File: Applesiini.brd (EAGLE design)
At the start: 63 x 69 mm, 55 parts

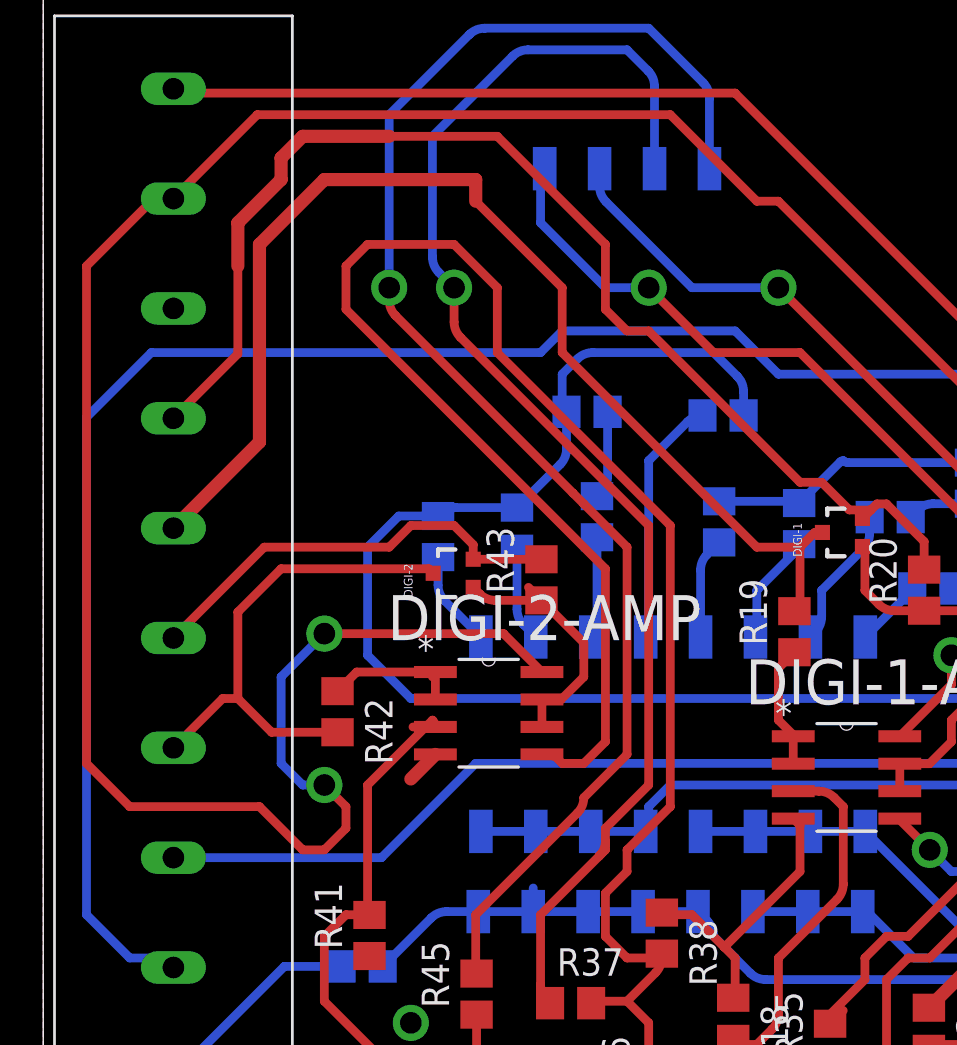
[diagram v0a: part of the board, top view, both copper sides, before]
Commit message: add correction to "Appelsiini" board
adds tolerance to one connection
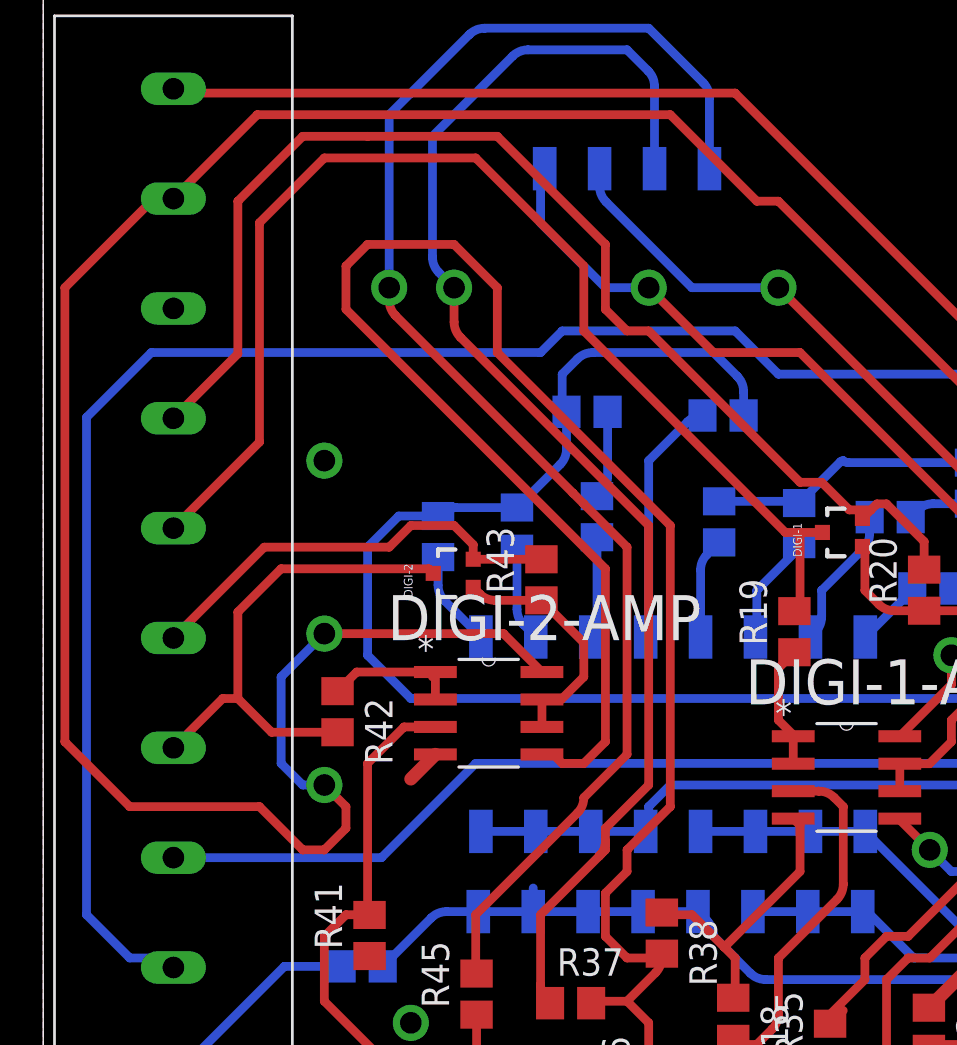
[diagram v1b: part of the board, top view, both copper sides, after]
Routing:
- net DIGI_LOW_1: track 56.9 -> 55.9 mm
- net DIGI_HIGH_1: track 54.8 -> 55.7 mm
- net N$64: track 12.2 -> 11.3 mm
- net VCC: track 216.3 -> 217.1 mm
- net N$11: track 33.0 -> 32.2 mm
- net GND: vias 6 -> 7

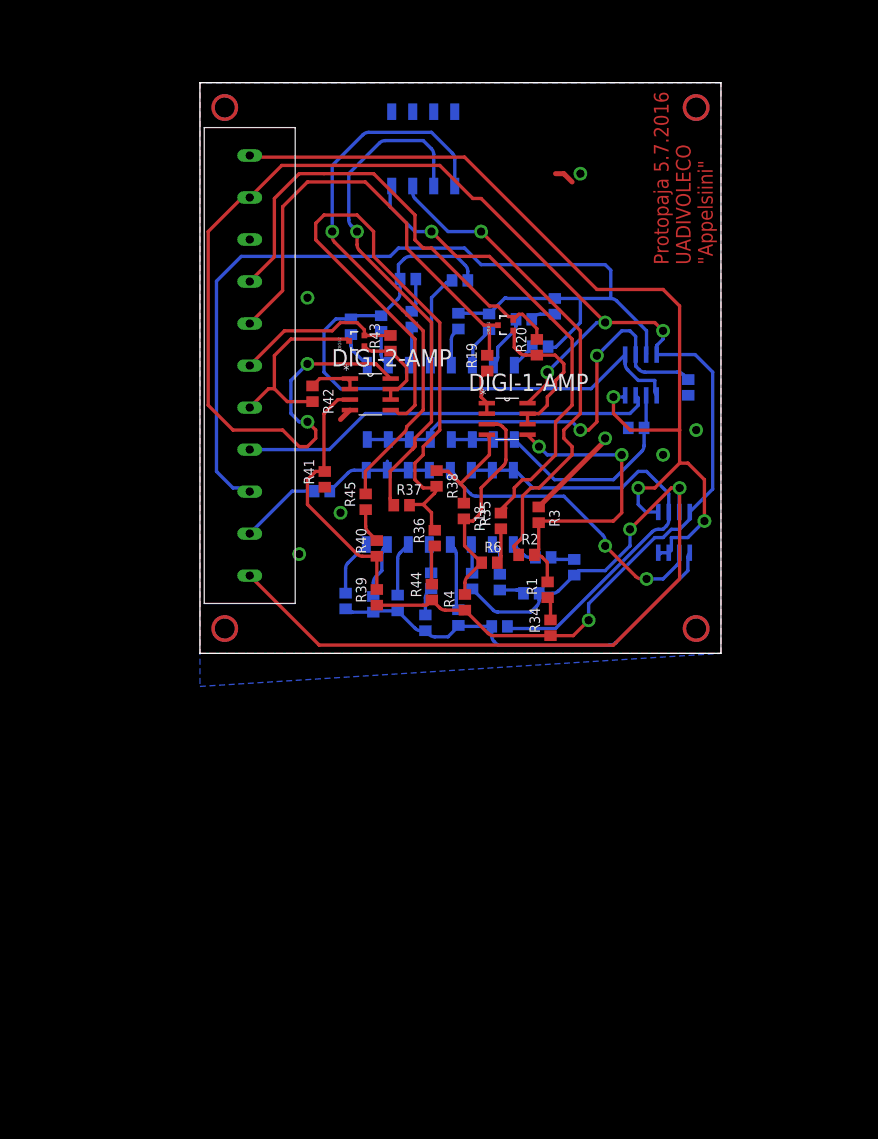
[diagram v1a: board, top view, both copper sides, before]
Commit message: add correction to "Appelsiini" board
gives more space around the board for easier matching of board sides.
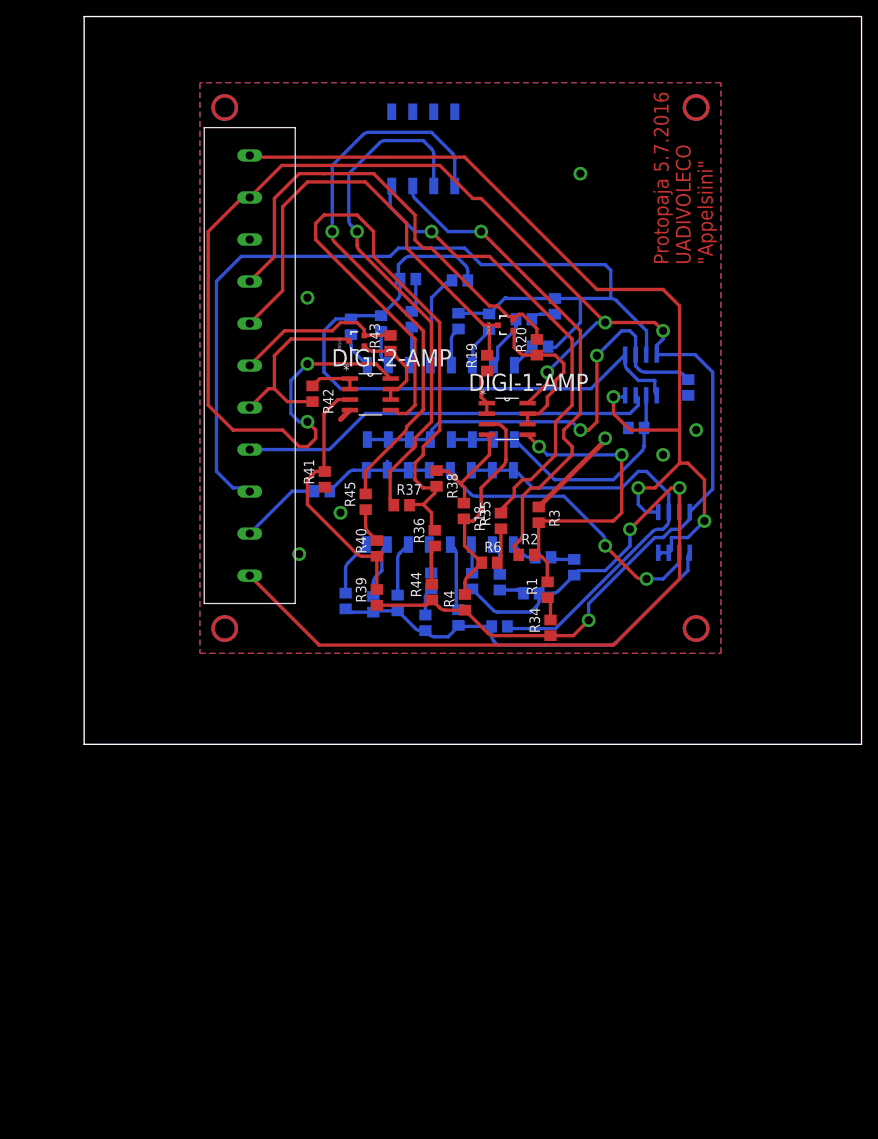
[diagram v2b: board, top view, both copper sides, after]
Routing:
- net GND: track 29.6 -> 27.2 mm
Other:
- board size 63 x 69 mm -> 94 x 88 mm
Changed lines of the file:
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@@
 <layer number="17" name="Pads" color="2" fill="1" visible="yes" active="yes"/>
 <layer number="18" name="Vias" color="2" fill="1" visible="yes" active="yes"/>
-<layer number="19" name="Unrouted" color="6" fill="1" visible="yes" active="yes"/>
+<layer number="19" name="Unrouted" color="6" fill="1" visible="no" active="yes"/>
 <layer number="20" name="Dimension" color="15" fill="1" visible="yes" active="yes"/>
 <layer number="21" name="tPlace" color="7" fill="1" visible="no" active="yes"/>
@@
 <board>
 <plain>
-<wire x1="0" y1="3" x2="63" y2="3" width="0" layer="20"/>
-<wire x1="63" y1="3" x2="63" y2="72" width="0" layer="20"/>
-<wire x1="63" y1="72" x2="0" y2="72" width="0" layer="20"/>
-<wire x1="0" y1="72" x2="0" y2="3" width="0" layer="20"/>
+<wire x1="-14" y1="-8" x2="80" y2="-8" width="0" layer="20"/>
+<wire x1="80" y1="-8" x2="80" y2="80" width="0" layer="20"/>
+<wire x1="80" y1="80" x2="-14" y2="80" width="0" layer="20"/>
+<wire x1="-14" y1="80" x2="-14" y2="-8" width="0" layer="20"/>
 <text x="62" y="50" size="1.778" layer="1" rot="R90">Protopaja 5.7.2016
 UADIVOLECO
@@
 <vertex x="63" y="72"/>
 </polygon>
-<wire x1="43" y1="61" x2="44" y2="61" width="0.6096" layer="1"/>
-<wire x1="44" y1="61" x2="45" y2="60" width="0.6096" layer="1"/>
 <wire x1="18.1362" y1="32.415" x2="17" y2="31.2788" width="0.6096" layer="1"/>
 <wire x1="40.96" y1="20.7" x2="49" y2="28.74" width="0.6096" layer="1"/>
@@
 <polygon width="0.254" layer="16" spacing="0.254" isolate="0.6096">
 <vertex x="0" y="72"/>
-<vertex x="0" y="-1"/>
+<vertex x="0" y="3"/>
 <vertex x="63" y="3"/>
 <vertex x="63" y="72"/>

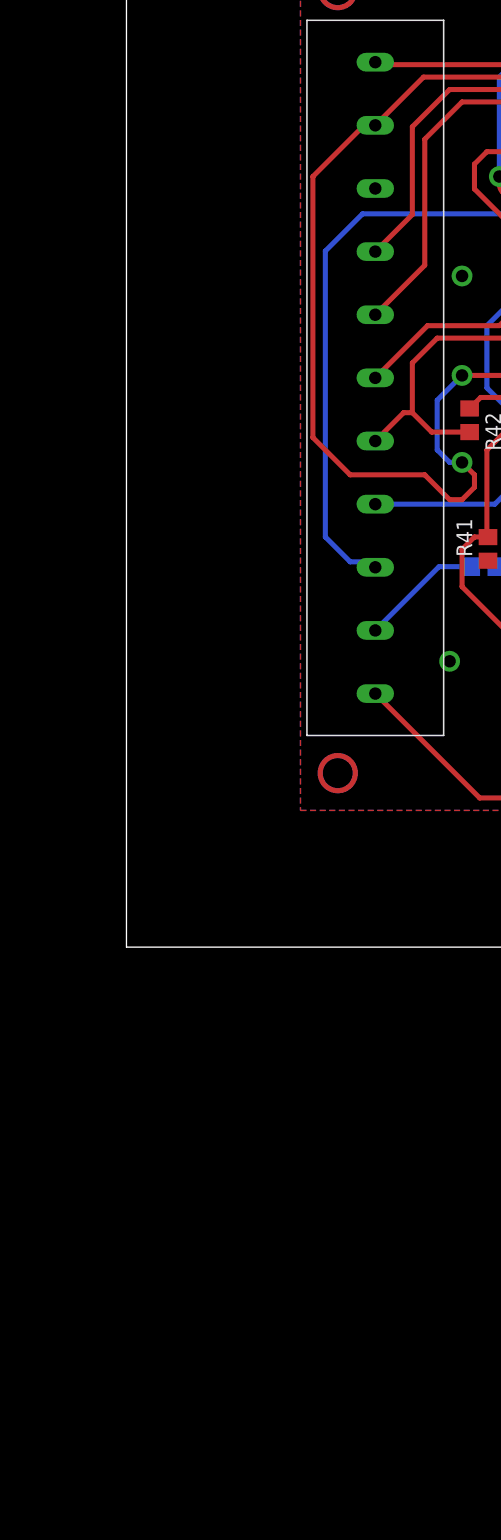
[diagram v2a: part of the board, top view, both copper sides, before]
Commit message: begin lime-lemon schematic and board
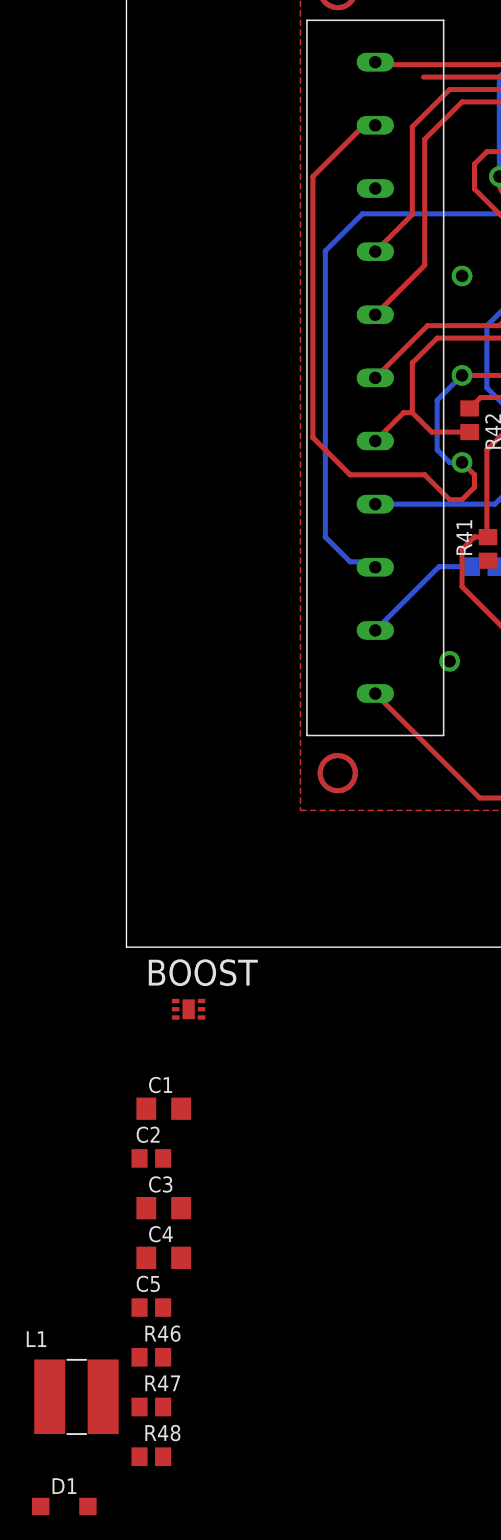
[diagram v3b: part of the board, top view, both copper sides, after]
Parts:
- added BOOST: TPS61170DRVT, Texas Instruments_By_element14_Batch_1:SON65P210X210X80-7N
- added C1, C3, C4: (no value), rcl:C1206
- added C2, C5: (no value), rcl:C0805
- added D1: (no value), diode:SOD123
- added L1: 22uH, SparkFun-Passives:SRN6045
- added R46, R47, R48: (no value), rcl:R0805
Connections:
- new net +5V: BOOST.5, BOOST.6, C2.1, L1.2, U$1.P$1
- new net N$44: BOOST.4, D1.A, L1.1
- new net N$47: D1.C, R47.2
- new net N$49: BOOST.2, R48.2
- new net N$51: C5.1, R48.1
- net GND: now also BOOST.3, C1.2, C2.2, C3.2, C4.2, C5.2, R46.2
- net VCC: now also BOOST.1, C1.1, C3.1, C4.1, R46.1, R47.1; no longer U$1.P$1
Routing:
- net VCC: track 217.1 -> 210.8 mm
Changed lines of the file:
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@@
 <element name="U$1" library="ruuviliitin" package="10KPL508" value="5.08PITCHTERMINAL" x="6.02" y="37.8" rot="R270"/>
 <element name="S4" library="smd-special" package="SMS-004" value="SWS004" x="27" y="64" rot="MR180"/>
+<element name="BOOST" library="Texas Instruments_By_element14_Batch_1" package="SON65P210X210X80-7N" value="TPS61170DRVT" x="-9" y="-13">
+<attribute name="PACKAGE" value="SON-6" x="-9" y="-13" size="1.778" layer="27" display="off"/>
+<attribute name="OC_FARNELL" value="1703404" x="-9" y="-13" size="1.778" layer="27" display="off"/>
+<attribute name="MPN" value="TPS61170DRVT" x="-9" y="-13" size="1.778" layer="27" display="off"/>
+<attribute name="SUPPLIER" value="Texas Instruments" x="-9" y="-13" size="1.778" layer="27" display="off"/>
+<attribute name="OC_NEWARK" value="65M6342" x="-9" y="-13" size="1.778" layer="27" display="off"/>
+</element>
+<element name="C1" library="rcl" package="C1206" value="" x="-11" y="-21"/>
+<element name="C2" library="rcl" package="C0805" value="" x="-12" y="-25"/>
+<element name="C3" library="rcl" package="C1206" value="" x="-11" y="-29"/>
+<element name="C4" library="rcl" package="C1206" value="" x="-11" y="-33"/>
+<element name="C5" library="rcl" package="C0805" value="" x="-12" y="-37"/>
+<element name="R46" library="rcl" package="R0805" value="" x="-12" y="-41"/>
+<element name="R47" library="rcl" package="R0805" value="" x="-12" y="-45"/>
+<element name="R48" library="rcl" package="R0805" value="" x="-12" y="-49"/>
+<element name="L1" library="SparkFun-Passives" package="SRN6045" value="22uH" x="-18" y="-44">
+<attribute name="PROD_ID" value="NDUC-11627" x="-18" y="-44" size="1.778" layer="27" display="off"/>
+</element>
+<element name="D1" library="diode" package="SOD123" value="" x="-19" y="-53"/>
 </elements>
 <signals>
@@
 <via x="56" y="27" extent="1-16" drill="1" diameter="1.6764"/>
 <via x="13" y="46" extent="1-16" drill="1" diameter="1.6764"/>
+<contactref element="C5" pad="2"/>
+<contactref element="C2" pad="2"/>
+<contactref element="BOOST" pad="3"/>
+<contactref element="R46" pad="2"/>
+<contactref element="C4" pad="2"/>
+<contactref element="C3" pad="2"/>
+<contactref element="C1" pad="2"/>
+<wire x1="30.81" y1="68.4958" x2="46" y2="61" width="0" layer="19" extent="16-16"/>
+<wire x1="28.27" y1="68.4958" x2="30.81" y2="68.4958" width="0" layer="19" extent="16-16"/>
+<wire x1="25.73" y1="68.4958" x2="28.27" y2="68.4958" width="0" layer="19" extent="16-16"/>
+<wire x1="23.19" y1="68.4958" x2="25.73" y2="68.4958" width="0" layer="19" extent="16-16"/>
+<wire x1="6.02" y1="53.04" x2="23.19" y2="68.4958" width="0" layer="19" extent="16-16"/>
+<wire x1="13" y1="46" x2="6.02" y2="53.04" width="0" layer="19" extent="1-1"/>
+<wire x1="18.1362" y1="32.415" x2="13" y2="46" width="0" layer="19" extent="1-1"/>
+<wire x1="15.09" y1="23.09" x2="17" y2="31.2788" width="0" layer="19" extent="1-1"/>
+<wire x1="17" y1="20" x2="15.09" y2="23.09" width="0" layer="19" extent="1-1"/>
+<wire x1="12" y1="15" x2="17" y2="20" width="0" layer="19" extent="1-1"/>
+<wire x1="28.61" y1="25.1" x2="17" y2="20" width="0" layer="19" extent="1-1"/>
+<wire x1="40.96" y1="20.7" x2="35" y2="27" width="0" layer="19" extent="1-1"/>
+<wire x1="51.8" y1="30.26" x2="49" y2="29" width="0" layer="19" extent="16-16"/>
+<wire x1="56" y1="27" x2="51.8" y2="30.26" width="0" layer="19" extent="16-16"/>
+<wire x1="60" y1="30" x2="56" y2="27" width="0" layer="19" extent="1-1"/>
+<wire x1="59.04" y1="34.2" x2="60" y2="30" width="0" layer="19" extent="16-16"/>
+<wire x1="-10.0414" y1="-13.6604" x2="12" y2="15" width="0" layer="19" extent="1-1"/>
+<wire x1="-9.6" y1="-21" x2="-10.0414" y2="-13.6604" width="0" layer="19" extent="1-1"/>
+<wire x1="-11.05" y1="-25" x2="-9.6" y2="-21" width="0" layer="19" extent="1-1"/>
+<wire x1="-9.6" y1="-29" x2="-11.05" y2="-25" width="0" layer="19" extent="1-1"/>
+<wire x1="-9.6" y1="-33" x2="-9.6" y2="-29" width="0" layer="19" extent="1-1"/>
+<wire x1="-11.05" y1="-37" x2="-9.6" y2="-33" width="0" layer="19" extent="1-1"/>
+<wire x1="-11.05" y1="-41" x2="-11.05" y2="-37" width="0" layer="19" extent="1-1"/>
 </signal>
 <signal name="VCC">
@@
 <contactref element="LOHI" pad="8"/>
 <contactref element="HILO" pad="8"/>
-<contactref element="U$1" pad="P$1"/>
 <contactref element="DIGI-2-AMP" pad="8"/>
 <contactref element="R39" pad="1"/>
@@
 <wire x1="59.225" y1="19.225" x2="59.225" y2="20.0938" width="0.4064" layer="16"/>
 <wire x1="34" y1="58" x2="49" y2="43" width="0.4064" layer="1"/>
-<wire x1="6.02" y1="58.12" x2="9.9" y2="62" width="0.4064" layer="1"/>
 <wire x1="9.9" y1="62" x2="29" y2="62" width="0.4064" layer="1"/>
 <wire x1="29" y1="62" x2="33" y2="58" width="0.4064" layer="1"/>
@@
 <wire x1="10" y1="30" x2="4" y2="30" width="0.4064" layer="1"/>
 <wire x1="1" y1="54" x2="5.12" y2="58.12" width="0.4064" layer="1"/>
-<wire x1="5.12" y1="58.12" x2="6.02" y2="58.12" width="0.4064" layer="1"/>
 <wire x1="1" y1="54" x2="1" y2="33" width="0.4064" layer="1"/>
 <wire x1="1" y1="33" x2="4" y2="30" width="0.4064" layer="1"/>
+<contactref element="R47" pad="1"/>
+<contactref element="BOOST" pad="1"/>
+<contactref element="R46" pad="1"/>
+<contactref element="C1" pad="1"/>
+<contactref element="C4" pad="1"/>
+<contactref element="C3" pad="1"/>
+<wire x1="-12.95" y1="-41" x2="-12.95" y2="-45" width="0" layer="19" extent="1-1"/>
+<wire x1="-12.4" y1="-33" x2="-12.95" y2="-41" width="0" layer="19" extent="1-1"/>
+<wire x1="-12.4" y1="-29" x2="-12.4" y2="-33" width="0" layer="19" extent="1-1"/>
+<wire x1="-12.4" y1="-21" x2="-12.4" y2="-29" width="0" layer="19" extent="1-1"/>
+<wire x1="-10.0414" y1="-12.3396" x2="-12.4" y2="-21" width="0" layer="19" extent="1-1"/>
+<wire x1="21.39" y1="8.82" x2="-10.0414" y2="-12.3396" width="0" layer="19" extent="1-1"/>
+<wire x1="5.12" y1="58.12" x2="9.9" y2="62" width="0" layer="19" extent="1-1"/>
 </signal>
 <signal name="DI-1">
@@
 <signal name="N$40">
 </signal>
+<signal name="+5V">
+<contactref element="BOOST" pad="6"/>
+<contactref element="BOOST" pad="5"/>
+<contactref element="C2" pad="1"/>
+<contactref element="L1" pad="2"/>
+<contactref element="U$1" pad="P$1"/>
+<wire x1="-7.9586" y1="-12.3396" x2="6.02" y2="58.12" width="0" layer="19" extent="1-1"/>
+<wire x1="-7.9586" y1="-13" x2="-7.9586" y2="-12.3396" width="0" layer="19" extent="1-1"/>
+<wire x1="-12.95" y1="-25" x2="-7.9586" y2="-13" width="0" layer="19" extent="1-1"/>
+<wire x1="-15.875" y1="-44.175" x2="-12.95" y2="-25" width="0" layer="19" extent="1-1"/>
+</signal>
+<signal name="N$44">
+<contactref element="L1" pad="1"/>
+<contactref element="D1" pad="A"/>
+<contactref element="BOOST" pad="4"/>
+<wire x1="-20.175" y1="-44.175" x2="-17.1" y2="-53" width="0" layer="19" extent="1-1"/>
+<wire x1="-7.9586" y1="-13.6604" x2="-20.175" y2="-44.175" width="0" layer="19" extent="1-1"/>
+</signal>
+<signal name="N$47">
+<contactref element="R47" pad="2"/>
+<contactref element="D1" pad="C"/>
+<wire x1="-11.05" y1="-45" x2="-20.9" y2="-53" width="0" layer="19" extent="1-1"/>
+</signal>
+<signal name="N$49">
+<contactref element="BOOST" pad="2"/>
+<contactref element="R48" pad="2"/>
+<wire x1="-10.0414" y1="-13" x2="-11.05" y2="-49" width="0" layer="19" extent="1-1"/>
+</signal>
+<signal name="N$51">
+<contactref element="R48" pad="1"/>
+<contactref element="C5" pad="1"/>
+<wire x1="-12.95" y1="-37" x2="-12.95" y2="-49" width="0" layer="19" extent="1-1"/>
+</signal>
 </signals>
